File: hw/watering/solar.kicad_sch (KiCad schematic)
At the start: 13 parts, among them U2 BQ25798

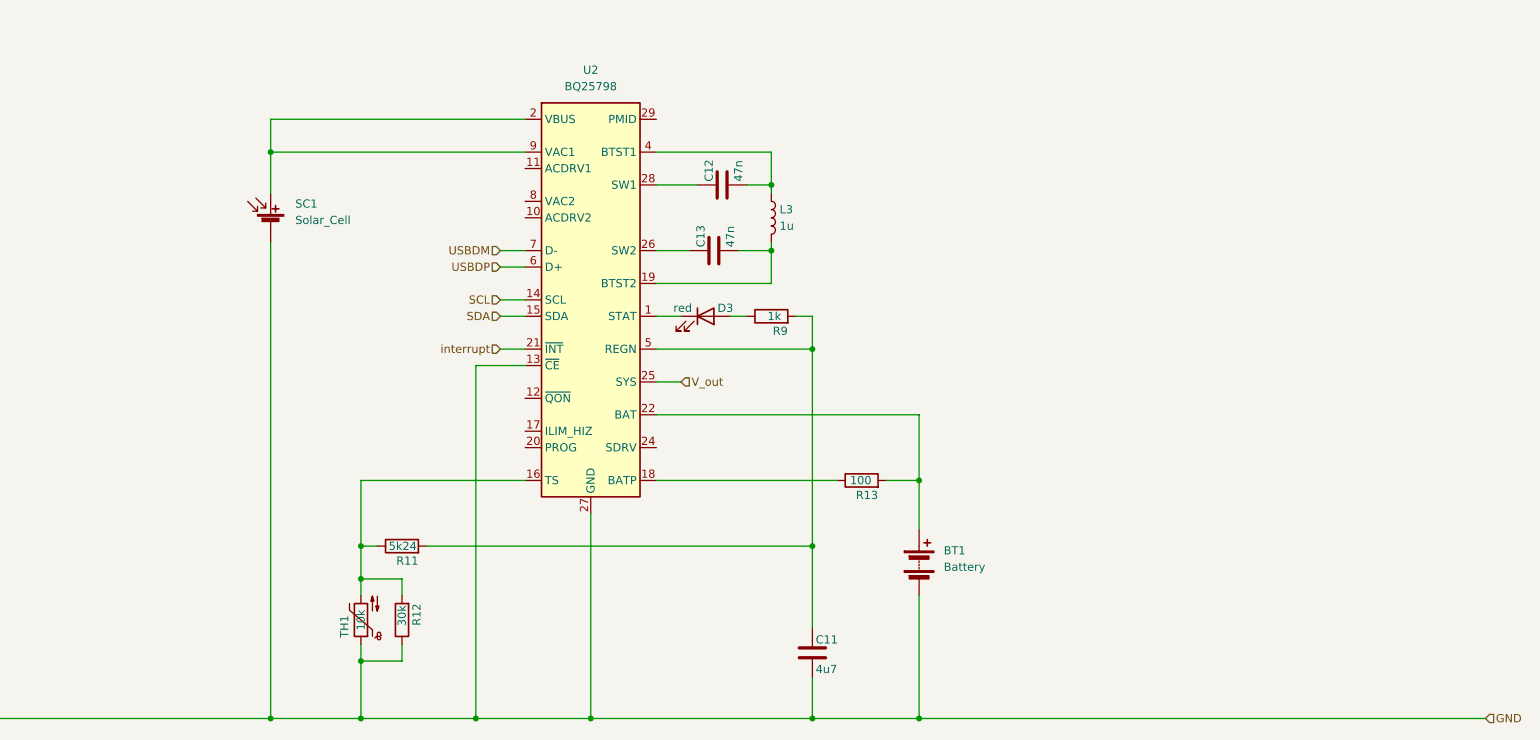
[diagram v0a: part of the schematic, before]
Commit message: added supply chip for battery and solar
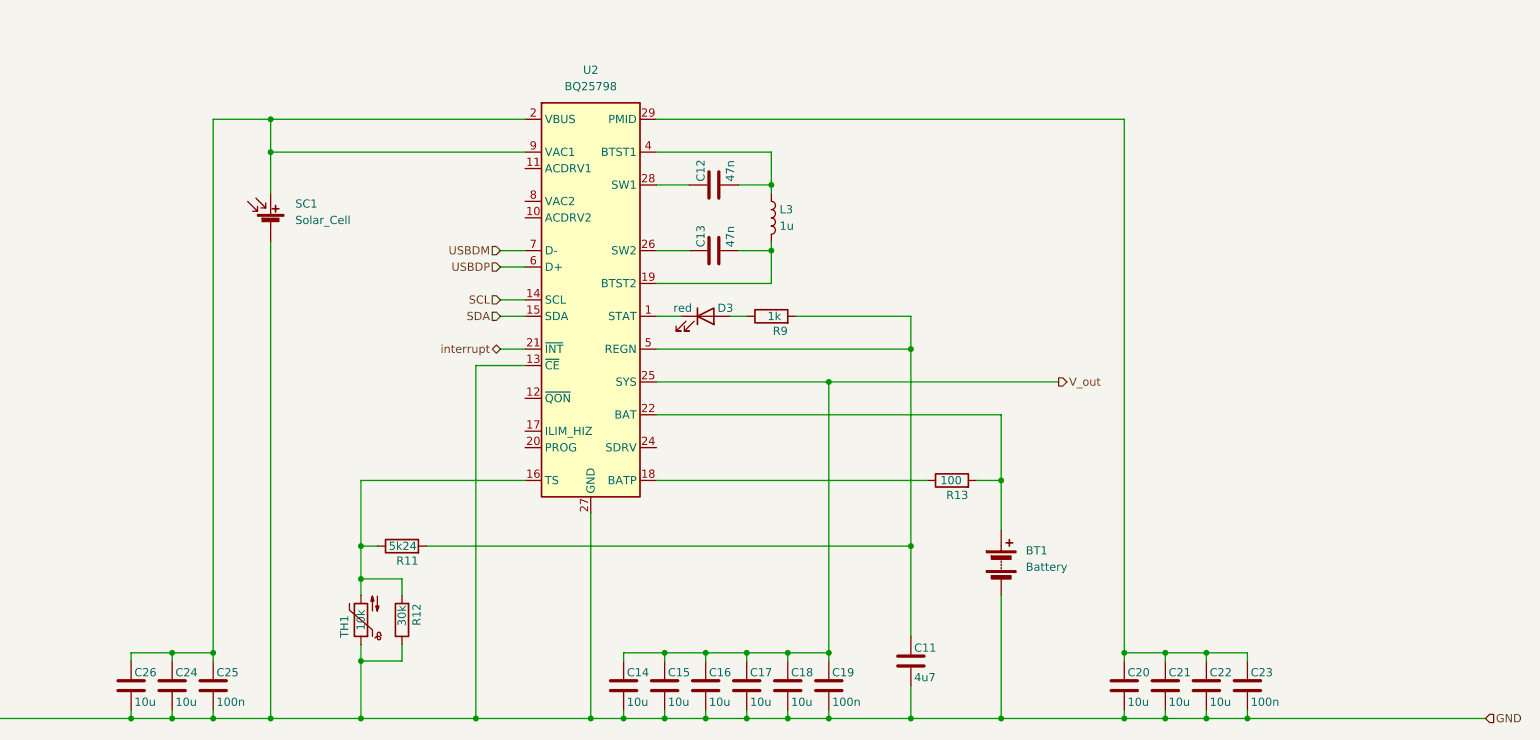
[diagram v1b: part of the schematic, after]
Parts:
- added C14, C15, C16, C17, C18, C20, C21, C22, C24, C26: 10u, Capacitor_SMD:C_0603_1608Metric, symbol Device:C
- added C19, C23, C25: 100n, Capacitor_SMD:C_0603_1608Metric, symbol Device:C
- BT1: footprint (none) -> Battery:BatteryHolder_Keystone_1042_1x18650
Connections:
- net GND: now also C14.2, C15.2, C16.2, C17.2, C18.2, C19.2, C20.2, C21.2, C22.2, C23.2, C24.2, C25.2, C26.2
- net V_out: now also C14.1, C15.1, C16.1, C17.1, C18.1, C19.1
- net at SC1.1 (+), U2.2 (VBUS), U2.3 (VBUS)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: now also C24.1, C25.1, C26.1
- net at U2.29 (PMID): now also C20.1, C21.1, C22.1, C23.1
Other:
- moved on the sheet: BT1, C11, C12, R13

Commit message: updated power
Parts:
- removed C13: 47n, Capacitor_SMD:C_0603_1608Metric, symbol Device:C
- removed C14, C15, C16, C17, C18, C20, C21, C22, C24: 10u, Capacitor_SMD:C_0603_1608Metric, symbol Device:C
- removed C19, C23, C25: 100n, Capacitor_SMD:C_0603_1608Metric, symbol Device:C
- removed D3: red, symbol Device:LED
- removed R12: 30k, Resistor_SMD:R_0603_1608Metric, symbol Device:R
- removed R13: 100, Resistor_SMD:R_0603_1608Metric, symbol Device:R
- removed TH1: 10k, symbol Device:Thermistor_NTC
- removed U2: BQ25798, Package_DFN_QFN:Texas_RQM0029A_VQFN-29_4x4mm_P0.4mm, symbol Battery_Management:BQ25798
- added BT2: 4V3, batteryholder:BH-18650-B1BA002, symbol Device:Battery
- added C31, C32: 22u, Capacitor_SMD:C_1206_3216Metric, symbol Device:C
- added D4, D5: SS210, Diode_SMD:D_SMA, symbol Device:D
- added L4: 22u, Inductor_SMD:L_Wuerth_MAPI-4030, symbol Device:L
- added U2: DRV8220DSG, Package_SON:WSON-8-1EP_2x2mm_P0.5mm_EP0.9x1.6mm, symbol Driver_Motor:DRV8220DSG
- added U3: NCP163AFCT330T2G, Package_CSP:WLCSP-4_0.64x0.64mm_Layout2x2_P0.35mm, symbol Regulator_Linear:NCP163AFCT330T2G
- added U5: STI3508, Package_TO_SOT_SMD:SOT-23-6, symbol sti3508:STI3508
- BT1: value Battery -> 4V3; footprint Battery:BatteryHolder_Keystone_1042_1x18650 -> batteryholder:BH-18650-B1BA002
- C11: value 4u7 -> 1u
- C12: value 47n -> 1u
- C26: value 10u -> 22u; footprint Capacitor_SMD:C_0603_1608Metric -> Capacitor_SMD:C_1206_3216Metric
- L3: value 1u -> 22u; footprint (none) -> Inductor_SMD:L_Wuerth_MAPI-4030
- R11: value 5k24 -> 45k
- R9: value 1k -> 10k
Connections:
- net +3V3: now also C12.1, R11.2, C32.1, D5.1 (K), U3.A2 (VOUT)
- net +5V: now also C11.1, U3.A1 (VIN), U3.B1 (EN)
- net +Vsolar: now also C26.1, SC1.1 (+), D4.1 (K), U2.1 (VM)
- net GND: now also C12.2, R9.2, BT2.2 (-), C31.2, C32.2, D4.2 (A), U2.4 (GND), U2.9 (GND), U3.B2 (GND), U5.2 (LX)
- net V_bat: now reaches L3.1
- net V_bat: now also BT1.1 (+), BT2.1 (+), C31.1, L4.2, U5.5 (V_in); no longer C12.2
- net 0V6: now reaches R9.1
- net 0V6: now also R11.1, U5.3 (FB)
- net at L3.2: now also D5.2 (A), U5.2 (LX)
- new net: L4.1, U2.2 (OUT1), U2.3 (OUT2)
- new net solar_enable: U2.8 (~{SLEEP})
- new net solar_pwm: U2.5 (IN2/EN), U2.6 (IN1/PH)
- new net v_en: U5.4 (EN)
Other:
- moved on the sheet: BT1, C26, SC1

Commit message: hardware progres
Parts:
- R11: value 45k -> 47k
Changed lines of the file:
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@@
 			)
 		)
-		(property "Datasheet" ""
+		(property "Datasheet" "https://jlc-prod-smt.oss-eu-central-1.aliyuncs.com/smtDataManualFile/8579706381316128768-C25804.pdf?response-content-disposition=attachment%3B%20filename%3DC25804.pdf%3B%20filename%2A%3DUTF-8%27%27C25804.pdf&x-oss-date=20260604T182440Z&x-oss-expires=1800&x-oss-security-token=CAISgAN1q6Ft5B2yfSjIr5nhDvTiu55L8aayRHLFsEERZtthpKj%2B0Dz2IHhMdHJsAOodtv0%2FmmhT6PkclqRLcbhpcmfjV%2BZHzLB8qeRniENA4J7b16cNrbH4M4H6aXeirtuwDsz9SNTCALjPD3nPii50x5bjaDymRCbLGJaViJlhHLN1Ow6jdmhpCctxLAlvo9NgFxm3D%2Fu2NQPwiWf9FVdhvhEG6Vly8qOi2MaRmFy8yFTx0b0SvJ%2BjYMrmPctoN9JnSdC5mfdzau3a1TJ84gRD0a5wkaVA1zbDs5bfISEIuUzebreLqY03dV4mOvdqIcMe8qigz88fk%2FfIioH6xyxKOexoSCnFTOiiupCcQLPyao9jLu6iayqViY7QaIOTqQohZmkAMwVOasAsI3Ngh4zF97Qt0cVNkXO9gWfLI8DtuMleWhri1Udu3tHD0eS19jklBdzSlusJRAJJUVBflCeKEaRNSAd3WGhEfM2%2BBt4QT30w5N2u00S8OSMIOONBvqKWD5sagAGpldF62iBeHzrNV%2BHnUyjaA64BCjacRbVbSjmxSgiuNX1d%2FbCnqQV25prdqNhtDbAKCoRnNQDFNxmhLIIUUcffM9eG3oRc44RNhyi7hADN6z1ILjt6TEoRuXkDAYH1u8iyrE2YQDMkq7F3Cke8dxQ44PYZqWefci6GHDzQ1pzPpiAA&x-oss-signature-version=OSS4-HMAC-SHA256&x-oss-credential=STS.NZTENVVAjFdYFTtTADjTMKmU2%2F20260604%2Feu-central-1%2Foss%2Faliyun_v4_request&x-oss-signature=78c2b620008555fdaf271c3d0b7682edd0aca7d23428d31f63338848e1713cab"
 			(at 250.19 148.59 0)
 			(hide yes)
@@
 			)
 		)
-		(property "Description" "Resistor"
+		(property "Description" "C25804"
 			(at 250.19 148.59 0)
 			(hide yes)
@@
 			)
 		)
-		(property "Value" "45k"
+		(property "Value" "47k"
 			(at 259.334 137.16 90)
 			(show_name no)
@@
 			)
 		)
-		(property "Datasheet" ""
+		(property "Datasheet" "https://jlc-prod-smt.oss-eu-central-1.aliyuncs.com/smtDataManualFile/8579706364622934016-C25819.pdf?response-content-disposition=attachment%3B%20filename%3DC25819.pdf%3B%20filename%2A%3DUTF-8%27%27C25819.pdf&x-oss-date=20260604T212703Z&x-oss-expires=1800&x-oss-security-token=CAISgAN1q6Ft5B2yfSjIr5qGBvnBmah58ZCnSW2IvnU%2FOOZNta3duzz2IHhMdHJsAOodtv0%2FmmhT6PkclqRLcbhpcmfjV%2BZHzLB8qc9%2FokVA4J7b16cNrbH4M4H6aXeirtuwDsz9SNTCALjPD3nPii50x5bjaDymRCbLGJaViJlhHLN1Ow6jdmhpCctxLAlvo9NgFxm3D%2Fu2NQPwiWf9FVdhvhEG6Vly8qOi2MaRmFy8yFTx0b0SvJ%2BjYMrmPctoN9JnSdC5mfdzau3a1TJ84gRD0a5wkaVA1zbDs5bfISEIuUzebreLqY03dV4mOvdqIcMe8qigz88fk%2FfIioH6xyxKOexoSCnFTOiiupCcQLPyao9jLu6iayqViY7QaIOTqQohZmkAMwVOasAsI3Ngh4zF97Qt0cVNkXO9gWfLI8DtuMleWqrvQN5iAnSgc5lCkRRYwGs1287ugXlSQzo890KPDAEovaKCnZ2ZSfh7Y4sNknI6i%2Bfc2Se2MIkILjrImKKWD5sagAFp6e2CTF5gXCAetl%2FZznzBeiqXvbdtrNp24XwBckBwOk4pCo9PLwSFMgOtQSf5U6kP%2F%2Bd1fI%2BKr022AwW2hsiCSfA6ItkAjrYqmnkpM1k6ce1E8ls7kKfeT%2Fq%2FikPDk77ij56kdNpXvKHTlexuI%2FHtV9DEGaEJEWVb894cTL2j2iAA&x-oss-signature-version=OSS4-HMAC-SHA256&x-oss-credential=STS.NY3MCutwXFRLKK9Zuj4iaZhvY%2F20260604%2Feu-central-1%2Foss%2Faliyun_v4_request&x-oss-signature=39443662dce0733909bc9974c7f7cc05e9a3997f7aeb5536bfa6dcd917da7abb"
 			(at 257.81 137.16 0)
 			(hide yes)
@@
 			)
 		)
-		(property "Description" "Resistor"
+		(property "Description" "C25819"
 			(at 257.81 137.16 0)
 			(hide yes)

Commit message: some progress on energy harvesting
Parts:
- removed C11, C12: 1u, Capacitor_SMD:C_0603_1608Metric, symbol Device:C
- removed U3: NCP163AFCT330T2G, Package_CSP:WLCSP-4_0.64x0.64mm_Layout2x2_P0.35mm, symbol Regulator_Linear:NCP163AFCT330T2G
- added L7: 22u, Inductor_SMD:L_Wuerth_MAPI-4030, symbol Device:L
- added R15, R28: 10k, Resistor_SMD:R_0603_1608Metric, symbol Device:R
- added R21: 39k, Resistor_SMD:R_0603_1608Metric, symbol Device:R
- added R27: 220k, Resistor_SMD:R_0603_1608Metric, symbol Device:R
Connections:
- net v_en is gone; now on net V_bat: U5.4 (EN)
- net +Vsolar: now also R27.2
- net GND: now also R15.2, R28.2
- net V_bat: now also R21.2; no longer L4.2
- net solar_pwm: no longer U2.5 (IN2/EN)
- net at L4.1, U2.2 (OUT1): no longer U2.3 (OUT2)
- new net: L7.1, U2.3 (OUT2)
- new net V_bat_meas: R15.1, R21.1
- new net current_meas/i_in: L4.2
- new net current_meas1/i_out: L7.2
- new net usb_pwm: U2.5 (IN2/EN)
- new net v_solar_meas: R27.1, R28.1
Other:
- added sheet current_meas (current_meas.kicad_sch)
- added sheet current_meas1 (current_meas.kicad_sch)
- added sheet ldo (ldo.kicad_sch)
- moved on the sheet: BT1, BT2, C26, C31, D4, L4, SC1, U2

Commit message: connections completet. started placing and routing
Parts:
- added C17, C18, C19: 1u, Capacitor_SMD:C_0603_1608Metric, symbol Device:C
- added R29: 47k, Resistor_SMD:R_0603_1608Metric, symbol Device:R
- added R30: 10k, Resistor_SMD:R_0603_1608Metric, symbol Device:R
- SC1: footprint (none) -> Capacitor_THT:CP_Axial_L20.0mm_D10.0mm_P26.00mm_Horizontal
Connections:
- net +5V: now also R29.2
- net GND: now also C17.2, C18.2, C19.2, R30.2
- net V_bat_meas: now also C18.1
- net solar_enable renamed pwm_enable
- net v_solar_meas renamed V_solar_meas
- net V_solar_meas: now also C17.1
- new net V_usb_meas: C19.1, R29.1, R30.1
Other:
- sheet current_meas ports: added V_in; removed +3V3
- sheet current_meas1 ports: added V_in; removed +3V3
- moved on the sheet: BT1, BT2, C26, C31, C32, D4, D5, L3, L4, L7, R11, R15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

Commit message: some more placing
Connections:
- net at D5.2 (A), L3.2: now also U5.1 (LX); no longer U5.2 (LX)

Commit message: routing done
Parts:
- removed C19: 1u, Capacitor_SMD:C_0603_1608Metric, symbol Device:C
- removed R29: 47k, Resistor_SMD:R_0603_1608Metric, symbol Device:R
- removed R30: 10k, Resistor_SMD:R_0603_1608Metric, symbol Device:R
- added C27, C36: 22u, Capacitor_SMD:C_1206_3216Metric, symbol Device:C
- SC1: footprint Capacitor_THT:CP_Axial_L20.0mm_D10.0mm_P26.00mm_Horizontal -> DORABO:DB142R-5.08-2P-GN
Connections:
- net +Vsolar: now also C27.1, C36.1
- net GND: now also C27.2, C36.2
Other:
- moved on the sheet: C17, D4, R27, R28
